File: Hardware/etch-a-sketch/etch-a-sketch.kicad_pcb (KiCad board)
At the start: 2 copper layers, 100 x 62 mm, 37 parts, among them J1 USART, J2 Conn_02x05_Odd_Even, J3 OLED, J4 Power Connector, SW1 Encoder 1, SW2 Encoder 2, U1 AMS1117-3.3, U2 STM32F401RET6

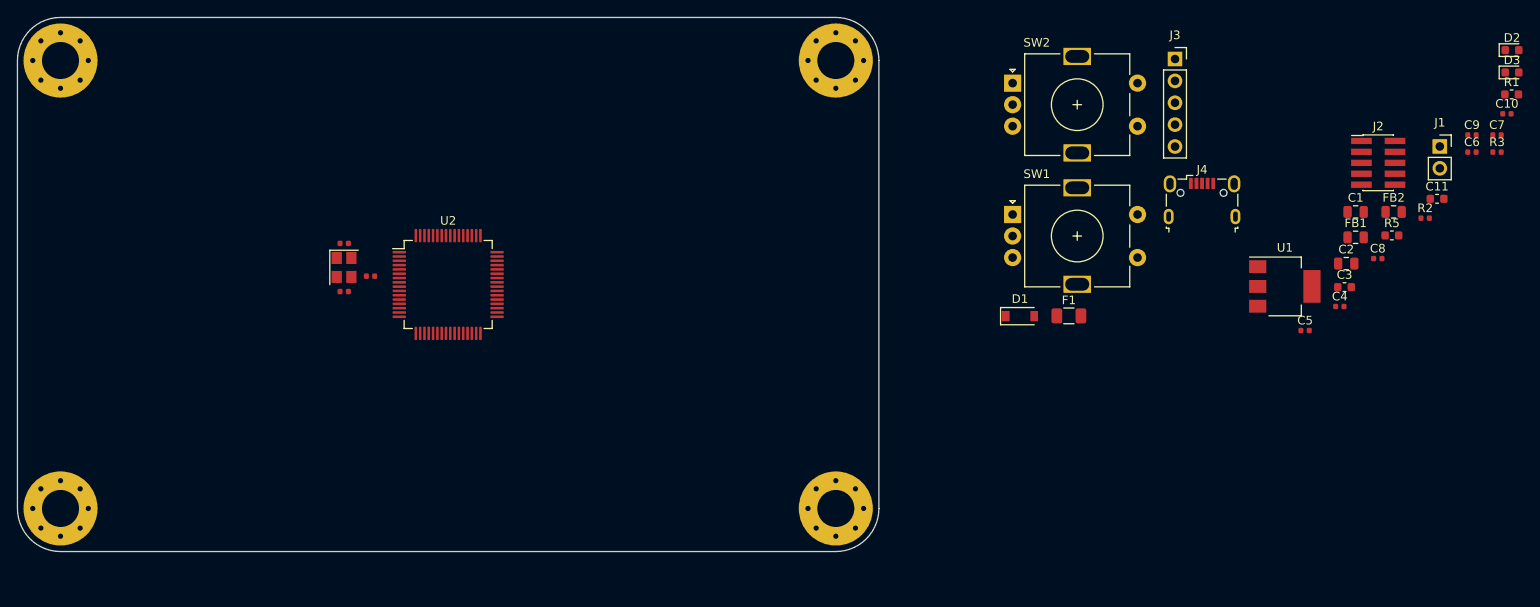
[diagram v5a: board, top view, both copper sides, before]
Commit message: feat: add decoupling capacitors
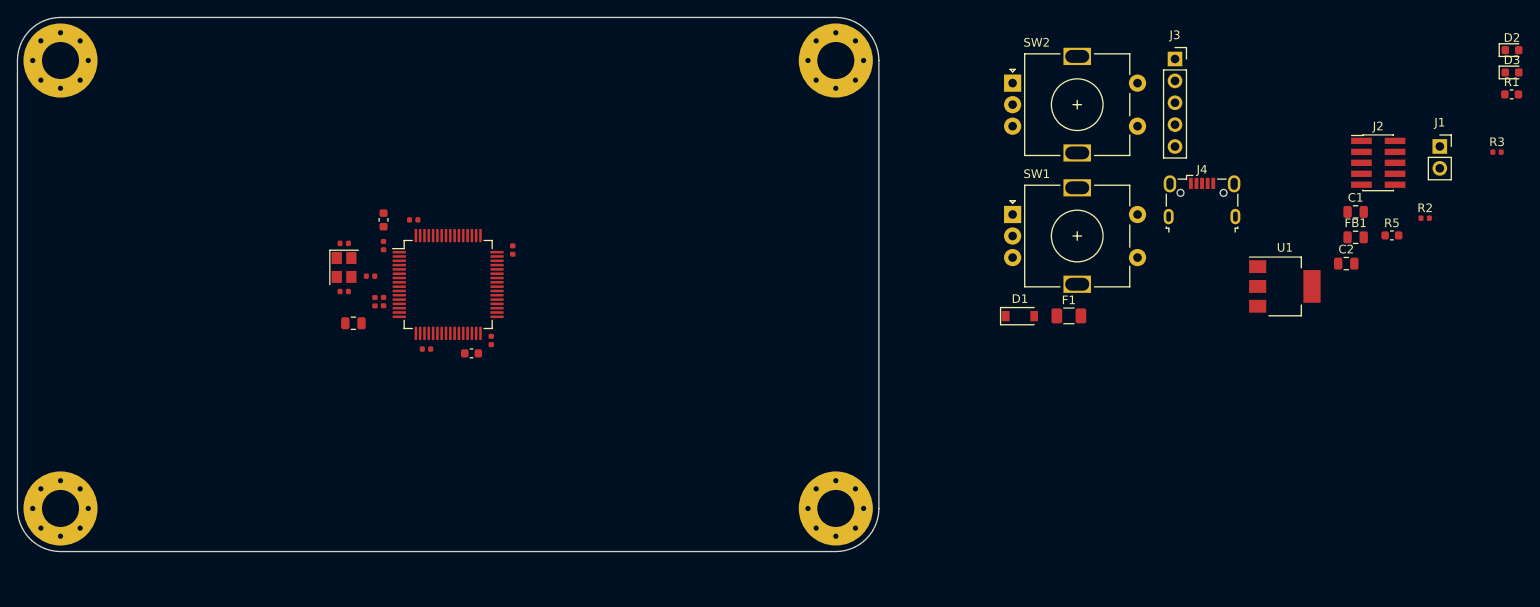
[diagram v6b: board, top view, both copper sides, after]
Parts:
- moved C10 133.2 mm to (61.5, 53.0), turned to 90 degrees
- moved C7 129.9 mm to (62.5, 46.5), turned to 90 degrees
- moved C9 127.8 mm to (62.5, 53.0), turned to 90 degrees
- moved FB2 121.4 mm to (59.0, 55.5), turned to 180 degrees
- moved C11 113.5 mm to (72.7, 59.0)
- moved C8 112.0 mm to (66.0, 43.5)
- moved C6 111.9 mm to (77.5, 47.0), turned to 270 degrees
- moved C3 111.8 mm to (62.5, 43.5), turned to 270 degrees
- moved C4 106.1 mm to (67.5, 58.5), turned to 180 degrees
- moved C5 94.5 mm to (75.0, 57.5), turned to 270 degrees

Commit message: feat: place encoders, refine placement of power regulator
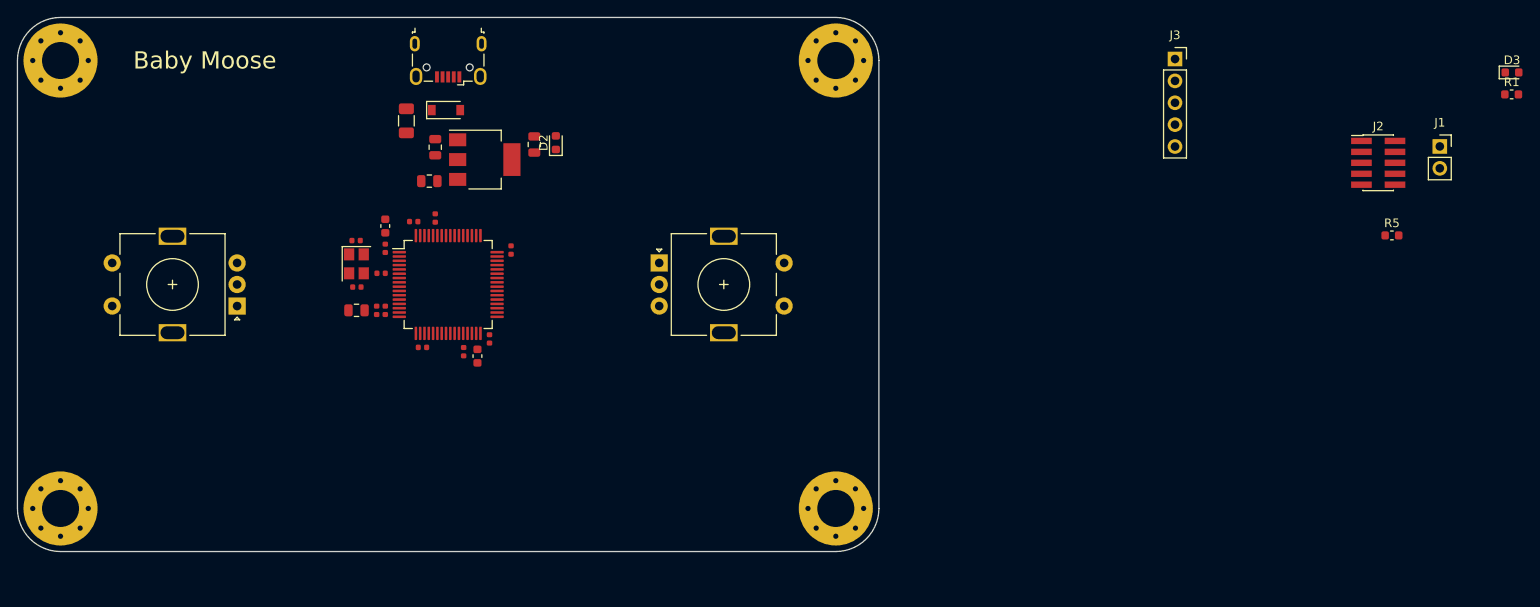
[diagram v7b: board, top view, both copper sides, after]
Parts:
- moved R3 122.2 mm to (71.8, 58.8), turned to 270 degrees
- moved R2 114.9 mm to (68.5, 43.3), turned to 90 degrees
- moved D2 111.5 mm to (82.5, 34.5), turned to 90 degrees
- moved FB1 107.7 mm to (67.8, 39.0), turned to 180 degrees
- moved C1 107.1 mm to (68.5, 35.1), turned to 90 degrees
- moved C2 95.3 mm to (80.0, 34.8), turned to 270 degrees
- moved U1 94.0 mm to (74.2, 36.5)
- moved SW2 93.7 mm to (45.5, 53.5), turned to 180 degrees
- moved J4 89.0 mm to (70.0, 25.0), turned to 180 degrees
- moved F1 80.2 mm to (65.2, 32.0), turned to 270 degrees
- moved D1 70.8 mm to (69.8, 30.8)
- moved SW1 41.4 mm to (94.5, 48.5)
- moved C13 1.55 mm to (59.4, 51.3)
- moved FB2 1.54 mm to (59.4, 54.0)
- moved HSE1 1.50 mm to (59.4, 48.6)
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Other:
- board text added: "Baby Moose"

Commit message: feat: place OLED socket
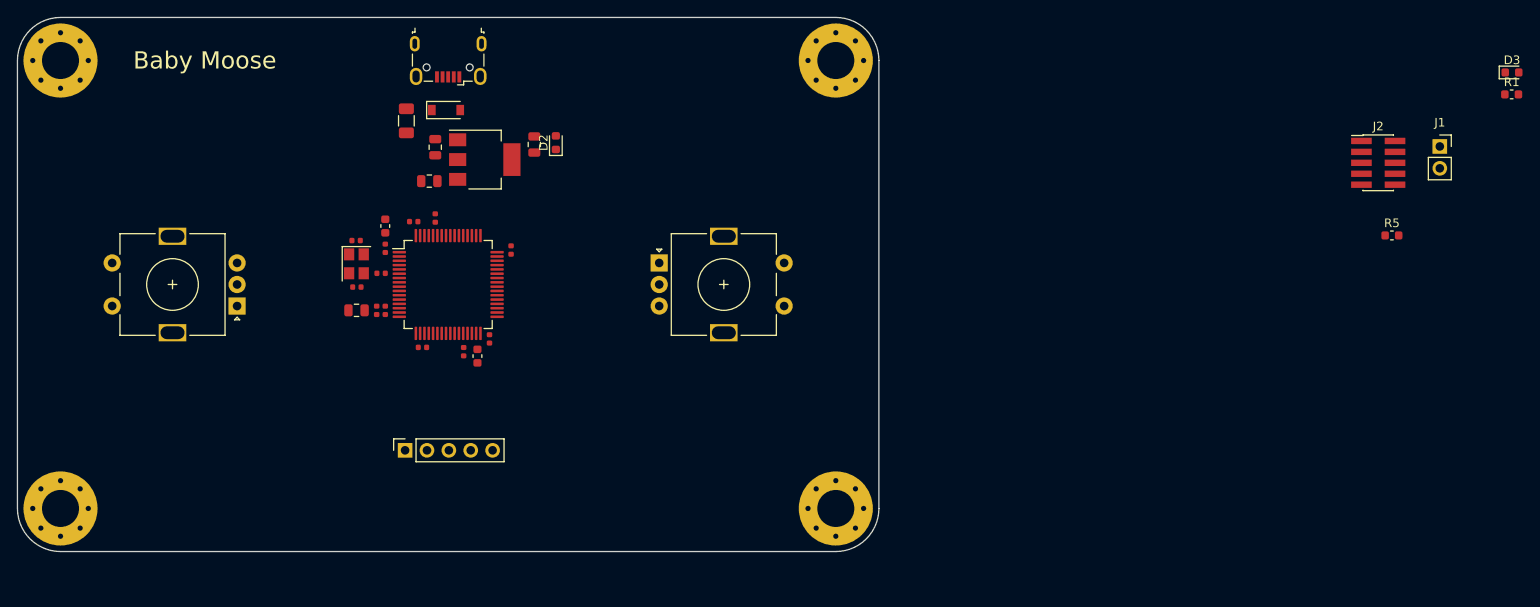
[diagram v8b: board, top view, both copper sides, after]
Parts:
- moved J3 100.3 mm to (65.0, 70.2), turned to 90 degrees
